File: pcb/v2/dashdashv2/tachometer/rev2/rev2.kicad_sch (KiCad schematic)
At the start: 182 parts, among them Q1 BSS138, Q2 BSS138, Q3 BSS138, Q4 BSS138, Q5 BSS138, Q6 BSS138, Q7 BSS138, U1 SK6812SIDE

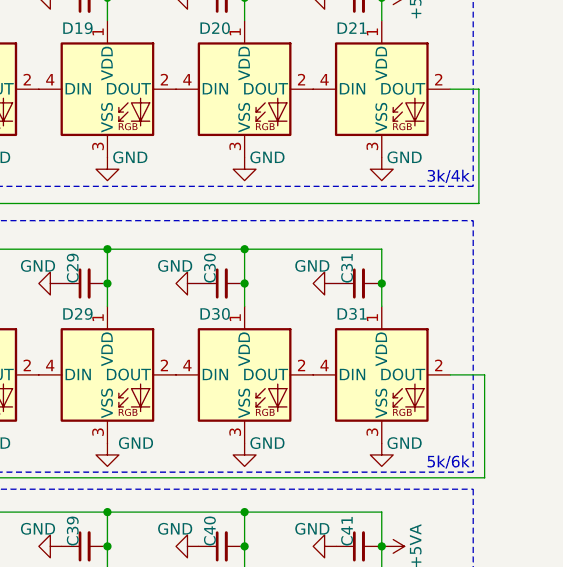
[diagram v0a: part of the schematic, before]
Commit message: routing neopixel
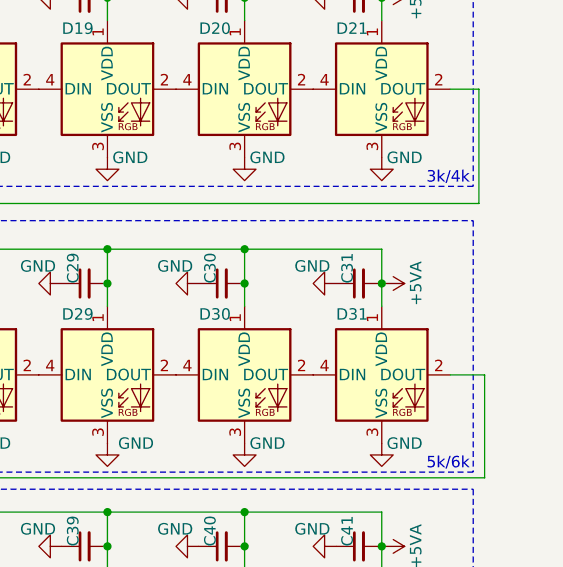
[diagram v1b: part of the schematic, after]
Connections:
- net +5VA: now also C27.2, C28.2, C29.2, C30.2, C31.2, D27.1 (VDD), D28.1 (VDD), D29.1 (VDD), D30.1 (VDD), D31.1 (VDD)
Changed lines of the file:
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@@
     (pin "1")
   )
+  (symbol (lib_id "power:+5VA") (at 264.795 84.455 270) (unit 1)
+    (in_bom yes) (on_board yes)
+    (property "Reference" "#PWR?" (id 0) (at 260.985 84.455 0)
+      (effects (font (size 1.27 1.27)) hide)
+    )
+    (property "Value" "+5VA" (id 1) (at 268.605 84.455 0))
+    (property "Footprint" "" (id 2) (at 264.795 84.455 0)
+      (effects (font (size 1.27 1.27)) hide)
+    )
+    (property "Datasheet" "" (id 3) (at 264.795 84.455 0)
+      (effects (font (size 1.27 1.27)) hide)
+    )
+    (pin "1")
+  )
   (symbol (lib_id "power:GND") (at 264.795 41.275 0) (unit 1)
     (in_bom yes) (on_board yes)
@@
       (reference "#PWR0105") (unit 1) (value "+12V") (footprint "")
     )
+    (path "/6a530ad6-adfb-4226-ac29-93e680a57268"
+      (reference "#PWR?") (unit 1) (value "+5VA") (footprint "")
+    )
     (path "/fa2e0bff-72e4-4530-8f69-dd23aa653bb6"

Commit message: tach v2, routing & 3D
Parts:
- removed C12, C13, C14, C15, C16, C17, C18, C19, C20, C21, C22, C23, C24, C25, C26, C27, C28, C29, C30, C31, C32, C33, C34, C35, C36, C37, C38, C39, C40, C41: 100nF, Capacitor_SMD:C_0805_2012Metric, symbol Device:C_Small
- removed D1, D10, D11, D12, D13, D14, D15, D16, D17, D18, D19, D2, D20, D21, D22, D23, D24, D25, D26, D27, D28, D29, D3, D30, D31, D32, D33, D34, D35, D36, D37, D38, D39, D4, D40, D41, D5, D6, D7, D8, D9: WS2812B, LED_SMD:LED_Cree-PLCC4_2x2mm_CW, symbol LED:WS2812B
- removed R12, R13, R2, R6: 1k 1/10W +-1%, Resistor_SMD:R_0603_1608Metric, symbol Device:R_Small
- removed U1: SK6812SIDE, symbol dashdashv2:SK6812SIDE
- added C53, C56: 100nF, Capacitor_SMD:C_0603_1608Metric, symbol Device:C_Small
- added C54, C55, C57: 30pF, Capacitor_SMD:C_0603_1608Metric, symbol Device:C_Small
- added C58: 2.2uF, Capacitor_SMD:C_0603_1608Metric, symbol Device:C_Small
- added D106: GREEN, LED_SMD:LED_0603_1608Metric, symbol Device:LED
- added D107: BLUE, LED_SMD:LED_0603_1608Metric, symbol Device:LED
- added D108: RED, LED_SMD:LED_0603_1608Metric, symbol Device:LED
- added D109: 1N4007, Diode_THT:D_DO-41_SOD81_P7.62mm_Horizontal, symbol Diode:1N4007
- added D110: BZV55B5V1, Diode_SMD:D_MiniMELF, symbol Diode:BZV55B5V1
- added H1, H2, H3, H4, H5, H6, H7, H8: MountingHole, MountingHole:MountingHole_2.2mm_M2_Pad, symbol Mechanical:MountingHole
- added H10: USB+, TestPoint:TestPoint_Pad_D1.5mm, symbol Mechanical:MountingHole_Pad
- added H11: USB_GND, TestPoint:TestPoint_Pad_D1.5mm, symbol Mechanical:MountingHole_Pad
- added H9: USB-, TestPoint:TestPoint_Pad_D1.5mm, symbol Mechanical:MountingHole_Pad
- added J1: Tag connect, Connector:Tag-Connect_TC2030-IDC-FP_2x03_P1.27mm_Vertical, symbol Connector_Generic:Conn_02x03_Odd_Even
- added J2: RPM_CONN1, Connector_PinHeader_1.27mm:PinHeader_2x05_P1.27mm_Vertical, symbol Connector_Generic:Conn_02x05_Odd_Even
- added J3: Conn_01x03, Connector_PinHeader_2.54mm:PinHeader_1x03_P2.54mm_Vertical, symbol Connector_Generic:Conn_01x03
- added JP1: BOOTSEL, Jumper:SolderJumper-2_P1.3mm_Open_TrianglePad1.0x1.5mm, symbol Jumper:SolderJumper_2_Open
- added R21: 10k, Resistor_SMD:R_0603_1608Metric, symbol Device:R
- added R22, R31, R34, R35: 1k, Resistor_SMD:R_0603_1608Metric, symbol Device:R
- added R32, R33: 27R, Resistor_SMD:R_0603_1608Metric, symbol Device:R
- added R36: 1k 1/10W +-1%, Resistor_SMD:R_0603_1608Metric, symbol Device:R_Small
- added R37: 330R 1/10W +-1%, Resistor_SMD:R_0603_1608Metric, symbol Device:R_Small
- added U1: W25Q128JVS, Package_SO:SOIC-8_5.23x5.23mm_P1.27mm, symbol Memory_Flash:W25Q128JVS
- added U2: LP5907MFX-3.3, Package_TO_SOT_SMD:SOT-23-5, symbol Regulator_Linear:LP5907MFX-3.3
- added U3: SRV05-4, Package_TO_SOT_SMD:SOT-23-6, symbol Power_Protection:SRV05-4
- added U4: RP2040, Package_DFN_QFN:QFN-56-1EP_7x7mm_P0.4mm_EP3.2x3.2mm, symbol rp2040:RP2040
- added U5: H11L1, Package_DIP:DIP-6_W7.62mm_Socket, symbol Isolator:H11L1
- added U6: YAAJ_DCDC_StepDown_LM2596, dashdash_lib:YAAJ_DCDC_StepDown_LM2596, symbol dashdashv2:YAAJ_DCDC_StepDown_LM2596
- added Y1: 12MHz, Crystal:Crystal_SMD_3225-4Pin_3.2x2.5mm, symbol Device:Crystal_GND24
- C1: value 100nF -> 2.2uF; footprint Capacitor_SMD:C_0805_2012Metric -> Capacitor_SMD:C_0603_1608Metric; LCSC C49678 -> (none)
- C10, C11, C2, C3, C4, C5, C6, C7, C8, C9: footprint Capacitor_SMD:C_0805_2012Metric -> Capacitor_SMD:C_0603_1608Metric; LCSC C49678 -> (none)
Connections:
- net BACK_2 is gone; now on net PWM_BACK_RPM: R7.2
- net BA_3_L is gone; now on net PWM_BACK_RPM: R14.2
- net BA_4_L is gone; now on net PWM_BACK_RPM: R11.2
- net +12V: no longer D102.2 (A), D46.2 (A), D47.2 (A), D58.2 (A), D62.2 (A), D66.2 (A), D70.2 (A), D74.2 (A), D78.2 (A), D82.2 (A), D86.2 (A), D90.2 (A), D94.2 (A), D98.2 (A)
- net +5VA: now also C56.1, U2.1 (IN), U2.3 (EN), U6.4 (Vout); no longer C1.2, C10.2, C11.2, C2.2, C3.2, C4.2, C5.2, C6.2, C7.2, C8.2, C9.2
- net BA_1: now also Q1.3 (D); no longer R1.1
- net BA_2: now also Q2.3 (D)
- net BA_3: now also Q7.3 (D)
- net BA_4: now also Q6.3 (D)
- net GND: now also C10.2, C11.2, C2.2, C3.2, C4.2, C5.2, C6.2, C7.2, C8.2, C9.2, C53.1, C54.1, C55.1, C56.2, C57.1, C58.1, D110.2 (A), H11.1, J1.5 (Pin_5), J2.10 (Pin_10), J2.9 (Pin_9), J3.3 (Pin_3), JP1.1 (A), R31.1, R34.1, R35.1, U1.4 (GND), U2.2 (GND), U3.2 (VN), U4.19 (TESTEN), U4.57 (GND), U5.2, U5.5, U6.2 (GND), U6.3 (GND), Y1.1, Y1.3; no longer C10.1, C11.1, C2.1, C3.1, C4.1, C5.1, C6.1, C7.1, C8.1, C9.1
- net LAUNCH: no longer R10.2
- net REV: no longer R8.2
- net SHIFT: no longer R9.2
- net at Q1.1 (G): now also R1.1
- net PWM_BACK_RPM: now reaches R1.2
- net PWM_BACK_RPM: now also J2.8 (Pin_8); no longer Q1.3 (D)
- new net: JP1.2 (B), R22.2
- new net: D109.1 (K), R36.1
- new net: D108.1 (K), R35.2
- new net: D110.1 (K), R36.2, R37.1
- new net: R37.2, U5.1
- new net: D107.1 (K), R34.2
- new net: D106.1 (K), R31.2
- new net +12LF: D102.2 (A), D46.2 (A), D47.2 (A), D58.2 (A), D62.2 (A), D66.2 (A), D70.2 (A), D74.2 (A), D78.2 (A), D82.2 (A), D86.2 (A), D90.2 (A), D94.2 (A), D98.2 (A), J2.1 (Pin_1), J2.2 (Pin_2), J3.1 (Pin_1), U6.1 (Vin)
- new net +1V1: C10.1, C11.1, C58.2, U4.23 (DVDD), U4.45 (VREG_VOUT), U4.50 (DVDD)
- new net +3V3: C1.2, C2.1, C3.1, C4.1, C5.1, C53.2, C57.2, C6.1, C7.1, C8.1, J1.1 (Pin_1), R21.2, U1.8 (VCC), U2.5 (OUT), U3.5 (VP), U4.1 (IOVDD), U4.10 (IOVDD), U4.22 (IOVDD), U4.26 (RUN), U4.33 (IOVDD), U4.42 (IOVDD), U4.44 (VREG_IN), U4.48 (USB_VDD), U4.49 (IOVDD), U5.6
- new net CLK: J2.3 (Pin_3), U3.1 (IO1), U4.27 (GPIO16)
- new net D+: R32.1, U4.46 (USB_DM)
- new net D-: R33.2, U4.47 (USB_DP)
- new net LAUNCH_L: R10.2
- new net LED_BLUE: D107.2 (A), U4.31 (GPIO20)
- new net LED_GREEN: D106.2 (A), U4.30 (GPIO19)
- new net LED_RED: D108.2 (A), U4.32 (GPIO21)
- new net MISO: J2.5 (Pin_5), U3.3 (IO2), U4.28 (GPIO17)
- new net MOSI: J2.7 (Pin_7), U3.6 (IO4), U4.29 (GPIO18)
- new net QSPI_SCLK: U1.6 (CLK), U4.52 (QSPI_SCLK)
- new net QSPI_SD0: U1.5 (DI(IO0)), U4.53 (QSPI_SD0)
- new net QSPI_SD1: U1.2 (DO(IO1)), U4.55 (QSPI_SD1)
- new net QSPI_SD2: U1.3 (IO2), U4.54 (QSPI_SD2)
- new net QSPI_SD3: U1.7 (IO3), U4.51 (QSPI_SD3)
- new net QSPI_SS: R21.1, R22.1, U1.1 (~{CS}), U4.56 (QSPI_SS)
- new net REV_L: R8.2
- new net RPM_CS: J2.4 (Pin_4), U3.4 (IO3), U4.2 (GPIO0)
- new net RPM_IN: D109.2 (A), J3.2 (Pin_2)
- new net RPM_OUT: U5.4
- new net SHIFT_L: R9.2
- new net SYS_SWCLK: J1.4 (Pin_4), U4.24 (SWCLK)
- new net SYS_SWDIO: J1.2 (Pin_2), U4.25 (SWD)
- new net USB_D+: H10.1, R33.1
- new net USB_D-: H9.1, R32.2
- new net VDDA: C9.1, U4.43 (ADC_AVDD)
- new net xin: C54.2, U4.20 (XIN), Y1.2
- new net xout: C55.2, U4.21 (XOUT), Y1.4
- no-connect marks 0 -> 5
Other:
- added sheet Tach (tach.kicad_sch)
- note added: "3V3 Source"
- note added: "ADC & USB"
- note added: "DVDD DECOUPLING"
- note added: "IOVDD DECOUPLING"
- note added: "TACH ADAPTER"
- note removed: "0/1000"
- note removed: "1k/2k"
- note removed: "2k/3k"
- note removed: "3k/4k"
- note removed: "4k/5k"
- note removed: "5k/6k"
- note removed: "6k/7k"
- note removed: "7k/8k"
- note removed: "SCH Binds"
- moved on the sheet: D100, D101, D102, D103, D104, D105, D42, D43, D44, D45, D46, D47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

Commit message: routing backlight leds
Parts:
- removed H4, H5: MountingHole, MountingHole:MountingHole_2.2mm_M2_Pad, symbol Mechanical:MountingHole
- removed R17, R19, R20: 1k 1/10W +-1%, Resistor_SMD:R_0603_1608Metric, symbol Device:R_Small
- added H4: USB_GND, TestPoint:TestPoint_Pad_D1.5mm, symbol Mechanical:MountingHole_Pad
- added Q8: BSS138, Package_TO_SOT_SMD:SOT-23, symbol Transistor_FET:BSS138
- added R12, R13, R2, R6: 1k 1/10W +-1%, Resistor_SMD:R_0603_1608Metric, symbol Device:R_Small
- D109: footprint Diode_THT:D_DO-41_SOD81_P7.62mm_Horizontal -> Diode_THT:D_DO-41_SOD81_P2.54mm_Vertical_AnodeUp; now in the parts list
- D110, J3, R36, R37, U5: now in the parts list
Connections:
- net BA_3: no longer R15.2, R16.2
- net CLK: now also U3.4 (IO3), U4.29 (GPIO18); no longer U3.1 (IO1), U4.27 (GPIO16)
- net GND: now also Q8.2 (S)
- net MOSI: now also U3.1 (IO1), U4.27 (GPIO16); no longer U3.6 (IO4), U4.29 (GPIO18)
- net PWM_BACK_RPM: now also R2.2
- net RPM_CS: now also U3.6 (IO4); no longer U3.4 (IO3)
- net TACH_DIN: now also H4.1
- net at D89.1 (K): now also R12.1; no longer R16.1
- net at D93.1 (K): now also R13.1
- net at D105.1 (K): now also R16.1
- net at D85.1 (K): now also R6.1; no longer R15.1
- net at D101.1 (K): now also R15.1
- new net: Q8.1 (G), R2.1
- new net BA_5: Q8.3 (D), R12.2, R13.2, R15.2, R16.2, R6.2
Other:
- moved on the sheet: D94, D95, D96, D97, Q1, R1, R18

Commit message: rpm routing v01
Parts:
- removed D102, D103, D104, D105: LED, LED_SMD:LED_0805_2012Metric, symbol Device:LED
- removed R16: 1k 1/10W +-1%, Resistor_SMD:R_0603_1608Metric, symbol Device:R_Small
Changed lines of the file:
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@@
   (junction (at 27.94 182.245) (diameter 0) (color 0 0 0 0)
   )
-  (junction (at 209.55 113.03) (diameter 0) (color 0 0 0 0)
-  )
   (junction (at 38.1 182.245) (diameter 0) (color 0 0 0 0)
   )
@@
     (stroke (width 0) (type default) (color 0 0 0 0))
   )
-  (wire (pts (xy 209.55 131.445) (xy 209.55 134.62))
-    (stroke (width 0) (type default) (color 0 0 0 0))
-  )
   (wire (pts (xy 118.745 83.82) (xy 118.745 86.36))
     (stroke (width 0) (type default) (color 0 0 0 0))
@@
     (stroke (width 0) (type solid) (color 0 0 0 0))
   )
-  (wire (pts (xy 209.55 120.65) (xy 209.55 123.825))
-    (stroke (width 0) (type default) (color 0 0 0 0))
-  )
   (wire (pts (xy 241.935 161.29) (xy 241.935 163.195))
     (stroke (width 0) (type default) (color 0 0 0 0))
@@
     (stroke (width 0) (type solid) (color 0 0 0 0))
   )
-  (wire (pts (xy 209.55 161.29) (xy 209.55 163.195))
-    (stroke (width 0) (type default) (color 0 0 0 0))
-  )
   (wire (pts (xy 257.81 113.03) (xy 260.35 113.03))
     (stroke (width 0) (type solid) (color 0 0 0 0))
@@
     (stroke (width 0) (type default) (color 0 0 0 0))
   )
-  (wire (pts (xy 209.55 153.035) (xy 209.55 156.21))
-    (stroke (width 0) (type default) (color 0 0 0 0))
-  )
   (wire (pts (xy 194.31 153.67) (xy 194.31 156.845))
     (stroke (width 0) (type default) (color 0 0 0 0))
@@
     (stroke (width 0) (type default) (color 0 0 0 0))
   )
-  (wire (pts (xy 209.55 142.24) (xy 209.55 145.415))
-    (stroke (width 0) (type default) (color 0 0 0 0))
-  )
   (wire (pts (xy 16.51 184.785) (xy 16.51 186.055))
     (stroke (width 0) (type default) (color 0 0 0 0))
@@
     (effects (font (size 1.27 1.27)) (justify left bottom))
   )
-  (text "BACKLIGTH" (at 208.28 115.57 270)
-    (effects (font (size 1.27 1.27)) (justify right bottom))
-  )
   (text "Launch Control" (at 264.16 90.805 270)
     (effects (font (size 0.8 0.8)) (justify right bottom))
@@
     (pin "2")
   )
-  (symbol (lib_id "Device:LED") (at 209.55 149.225 90) (unit 1)
-    (in_bom yes) (on_board yes)
-    (property "Reference" "D105" (id 0) (at 209.423 146.8754 90)
-      (effects (font (size 1.27 1.27)) (justify right))
-    )
-    (property "Value" "LED" (id 1) (at 212.598 151.3204 90)
-      (effects (font (size 1.27 1.27)) (justify right) hide)
-    )
-    (property "Footprint" "LED_SMD:LED_0805_2012Metric" (id 2) (at 209.55 149.225 0)
-      (effects (font (size 1.27 1.27)) hide)
-    )
-    (property "Datasheet" "~" (id 3) (at 209.55 149.225 0)
-      (effects (font (size 1.27 1.27)) hide)
-    )
-    (property "LCSC" "C205447" (id 4) (at 209.55 149.225 90)
-      (effects (font (size 1.27 1.27)) hide)
-    )
-    (pin "1")
-    (pin "2")
-  )
   (symbol (lib_id "power:+5VA") (at 233.68 25.4 0) (unit 1)
     (in_bom yes) (on_board yes)
@@
     (pin "2")
   )
-  (symbol (lib_id "Device:LED") (at 209.55 127.635 90) (unit 1)
-    (in_bom yes) (on_board yes)
-    (property "Reference" "D103" (id 0) (at 209.423 125.2854 90)
-      (effects (font (size 1.27 1.27)) (justify right))
-    )
-    (property "Value" "LED" (id 1) (at 212.598 129.7304 90)
-      (effects (font (size 1.27 1.27)) (justify right) hide)
-    )
-    (property "Footprint" "LED_SMD:LED_0805_2012Metric" (id 2) (at 209.55 127.635 0)
-      (effects (font (size 1.27 1.27)) hide)
-    )
-    (property "Datasheet" "~" (id 3) (at 209.55 127.635 0)
-      (effects (font (size 1.27 1.27)) hide)
-    )
-    (property "LCSC" "C205447" (id 4) (at 209.55 127.635 90)
-      (effects (font (size 1.27 1.27)) hide)
-    )
-    (pin "1")
-    (pin "2")
-  )
   (symbol (lib_id "power:GND") (at 48.895 149.86 0) (unit 1)
     (in_bom yes) (on_board yes)
@@
     (pin "1")
   )
-  (symbol (lib_id "Device:R_Small") (at 209.55 158.75 0) (unit 1)
-    (in_bom yes) (on_board yes)
-    (property "Reference" "R16" (id 0) (at 211.0486 157.5816 0)
-      (effects (font (size 1.27 1.27)) (justify left))
-    )
-    (property "Value" "1k 1/10W +-1%" (id 1) (at 205.74 171.45 90)
-      (effects (font (size 1.27 1.27)) (justify left) hide)
-    )
-    (property "Footprint" "Resistor_SMD:R_0603_1608Metric" (id 2) (at 209.55 158.75 0)
-      (effects (font (size 1.27 1.27)) hide)
-    )
-    (property "Datasheet" "~" (id 3) (at 209.55 158.75 0)
-      (effects (font (size 1.27 1.27)) hide)
-    )
-    (property "LCSC" "C217840" (id 4) (at 209.55 158.75 0)
-      (effects (font (size 1.27 1.27)) hide)
-    )
-    (pin "1")
-    (pin "2")
-  )
   (symbol (lib_id "Device:C_Small") (at 38.1 187.325 0) (unit 1)
     (in_bom yes) (on_board yes)
@@
     (pin "2")
   )
-  (symbol (lib_id "Device:LED") (at 209.55 116.84 90) (unit 1)
-    (in_bom yes) (on_board yes)
-    (property "Reference" "D102" (id 0) (at 209.423 114.4904 90)
-      (effects (font (size 1.27 1.27)) (justify right))
-    )
-    (property "Value" "LED" (id 1) (at 212.598 118.9354 90)
-      (effects (font (size 1.27 1.27)) (justify right) hide)
-    )
-    (property "Footprint" "LED_SMD:LED_0805_2012Metric" (id 2) (at 209.55 116.84 0)
-      (effects (font (size 1.27 1.27)) hide)
-    )
-    (property "Datasheet" "~" (id 3) (at 209.55 116.84 0)
-      (effects (font (size 1.27 1.27)) hide)
-    )
-    (property "LCSC" "C205447" (id 4) (at 209.55 116.84 90)
-      (effects (font (size 1.27 1.27)) hide)
-    )
-    (pin "1")
-    (pin "2")
-  )
   (symbol (lib_id "Device:LED") (at 257.175 101.6 90) (unit 1)
     (in_bom no) (on_board no)
@@
     (pin "1")
   )
-  (symbol (lib_id "Device:LED") (at 209.55 138.43 90) (unit 1)
-    (in_bom yes) (on_board yes)
-    (property "Reference" "D104" (id 0) (at 209.423 136.0804 90)
-      (effects (font (size 1.27 1.27)) (justify right))
-    )
-    (property "Value" "LED" (id 1) (at 212.598 140.5254 90)
-      (effects (font (size 1.27 1.27)) (justify right) hide)
-    )
-    (property "Footprint" "LED_SMD:LED_0805_2012Metric" (id 2) (at 209.55 138.43 0)
-      (effects (font (size 1.27 1.27)) hide)
-    )
-    (property "Datasheet" "~" (id 3) (at 209.55 138.43 0)
-      (effects (font (size 1.27 1.27)) hide)
-    )
-    (property "LCSC" "C205447" (id 4) (at 209.55 138.43 90)
-      (effects (font (size 1.27 1.27)) hide)
-    )
-    (pin "1")
-    (pin "2")
-  )
   (symbol (lib_id "Transistor_FET:BSS138") (at 35.56 167.64 0) (mirror y) (unit 1)
     (in_bom no) (on_board no)
@@
       (reference "D101") (unit 1) (value "LED") (footprint "LED_SMD:LED_0805_2012Metric")
     )
-    (path "/cc8baffb-5db8-4cac-a510-0773d787b848"
-      (reference "D102") (unit 1) (value "LED") (footprint "LED_SMD:LED_0805_2012Metric")
-    )
-    (path "/728c78e9-2b86-46d1-aed6-58dc50f27d1c"
-      (reference "D103") (unit 1) (value "LED") (footprint "LED_SMD:LED_0805_2012Metric")
-    )
-    (path "/f145ca3c-6ae8-4501-815f-a341aeaeeca5"
-      (reference "D104") (unit 1) (value "LED") (footprint "LED_SMD:LED_0805_2012Metric")
-    )
-    (path "/669b7234-78fd-43f9-b541-03e4c631b86f"
-      (reference "D105") (unit 1) (value "LED") (footprint "LED_SMD:LED_0805_2012Metric")
-    )
     (path "/e98b5c7f-4981-4dea-af05-26a2a3190e2a"
       (reference "D106") (unit 1) (value "GREEN") (footprint "LED_SMD:LED_0603_1608Metric")
@@
       (reference "R15") (unit 1) (value "1k 1/10W +-1%") (footprint "Resistor_SMD:R_0603_1608Metric")
     )
-    (path "/b04881dc-70ed-4fdd-ae42-6739db697ca4"
-      (reference "R16") (unit 1) (value "1k 1/10W +-1%") (footprint "Resistor_SMD:R_0603_1608Metric")
-    )
     (path "/70b37768-3936-438b-a999-07669204de79"

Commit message: update neopixel
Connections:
- net TACH_DIN: now also U4.14 (GPIO11)
